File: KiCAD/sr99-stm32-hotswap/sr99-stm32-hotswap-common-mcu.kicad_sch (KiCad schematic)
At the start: 52 parts, among them J1 UDB, J2 Conn_01x02, Q1 2N7002, Q2 2N7002, Q3 2N7002, U1 STM32G474CBTx, U12 M25C-MEM-SPI, U2 MC74HC589AD, U3 MC74HC589AD, U4 MC74HC589AD, U5 AP2112K, Y1 8Mhz SMD3225-4P

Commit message: wip-2025-11-19
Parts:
- added J2: ~, Connector_JST:JST_SH_SM04B-SRSS-TB_1x04-1MP_P1.00mm_Horizontal, symbol ts-kicad-lib:QWIIC
- added J3: TC2030_SWD, PCM_marbastlib-various:CON_TC2030_outlined, symbol PCM_marbastlib-various:TC2030_SWD
- D1: footprint (none) -> Diode_SMD:D_SOD-323_HandSoldering
- renumbered C3 to C1, C9 to C10, C10 to C11, C11 to C12, C12 to C13, C13 to C14, C14 to C15, C15 to C16, C16 to C17, C17 to C18, C18 to C19, C19 to C20, C1 to C3, C38 to C9, J2 to J4, U12 to U5, U5 to U6
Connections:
- net +3V3: now also C1.2, C2.2, C3.2, J2.2, J3.1 (VCC); no longer C1.1, C10.1, C11.1, C12.1, C13.1, C14.1, C15.1, C16.1, C17.1, C18.1, C19.1, C2.1, C20.1, C3.1, C4.1, C5.1, C6.1, C7.1, C8.1, C9.1, J1.4, J1.MP, Q1.2 (S), Q2.2 (S), Q3.2 (S), R1.1, R1.3, R1.5, R1.7, R14.1, R15.1, R2.1, R2.3, R2.5, R2.7, R3.1, R3.3, R3.5, R3.7, R4.1, R4.3, R4.5, R4.7, R5.1, R5.3, R5.5, R5.7, R6.1, R9.1, U1.19 (VSSA), U1.23 (VSS), U1.35 (VSS), U1.47 (VSS), U2.14 (SA), U2.8 (GND), U3.8 (GND), U4.8 (GND), U5.4 (GND), U5.9 (Pad), U6.2 (GND), Y1.2, Y1.4
- net ~{RST}: now also J3.3 (~{RST})
- net PA13 renamed SWDIO
- net SWDIO: now also J3.2 (SWDIO)
- net PA14 renamed SWCLK
- net SWCLK: now also J3.4 (SWCLK)
- net PA15 renamed SCL
- net PB7 renamed SDA
- new net GND: C1.1, C10.1, C11.1, C12.1, C13.1, C14.1, C15.1, C16.1, C17.1, C18.1, C19.1, C2.1, C20.1, C3.1, C4.1, C5.1, C6.1, C7.1, C8.1, C9.1, J1.4, J1.MP, J2.1, J2.MP, J3.5 (GND), Q1.2 (S), Q2.2 (S), Q3.2 (S), R1.1, R1.3, R1.5, R1.7, R14.1, R15.1, R2.1, R2.3, R2.5, R2.7, R3.1, R3.3, R3.5, R3.7, R4.1, R4.3, R4.5, R4.7, R5.1, R5.3, R5.5, R5.7, R6.1, R9.1, U1.19 (VSSA), U1.23 (VSS), U1.35 (VSS), U1.47 (VSS), U2.14 (SA), U2.8 (GND), U3.8 (GND), U4.8 (GND), U5.4 (GND), U5.9 (Pad), U6.2 (GND), Y1.2, Y1.4
- new net SWSCL: J3.6 (SWO)
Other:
- note added: "Connectors"
- note removed: "UDB"
- moved on the sheet: J1

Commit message: update-2025-11-20
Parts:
- added R37, R38: 4K7, Resistor_SMD:R_0603_1608Metric, symbol Device:R_Small
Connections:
- net +3V3: now also R37.2, R38.2
- net COL0: now also R4.7; no longer R4.4
- net COL10: now also R2.8; no longer R2.2
- net COL11: now also R2.7; no longer R2.4
- net COL13: now also R2.5; no longer R2.8
- net COL14: now also R3.8; no longer R3.2
- net COL15: now also R3.7; no longer R3.4
- net COL17: now also R3.5; no longer R3.8
- net COL2: now also R4.5; no longer R4.8
- net COL3: now also R1.8; no longer R1.2
- net COL4: now also R1.7; no longer R1.4
- net COL6: now also R1.5; no longer R1.8
- net COL7: now also R5.7; no longer R5.4
- net COL9: now also R5.5; no longer R5.8
- net GND: now also R1.2, R1.3, R1.4, R2.2, R2.3, R2.4, R3.2, R3.3, R3.4, R4.2, R4.3, R4.4, R5.2, R5.3, R5.4; no longer R1.3, R1.5, R1.7, R2.3, R2.5, R2.7, R3.3, R3.5, R3.7, R4.3, R4.5, R4.7, R5.3, R5.5, R5.7
- net SCL: now also J2.4, R37.1
- net SDA: now also J2.3, R38.1
- net at U2.15 (A): now also R4.8; no longer R4.2
- net at U3.15 (A): now also R5.8; no longer R5.2
- net PB10: no longer names the net of U1.22 (PB10)
- no-connect marks 0 -> 1
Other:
- moved on the sheet: C13, C4, D1, J1, J3, J4, Q2, Q3, R10, R12, R13, R14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

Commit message: wip-2025-11-23
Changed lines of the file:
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@@
 		)
 		(property "Value" "MC74HC589AD"
-			(at 273.304 73.66 0)
+			(at 271.78 73.66 0)
 			(effects
 				(font
@@
 		)
 		(property "Value" "MC74HC589AD"
-			(at 235.204 73.66 0)
+			(at 233.68 73.66 0)
 			(effects
 				(font
@@
 		)
 		(property "Value" "MC74HC589AD"
-			(at 197.104 73.66 0)
+			(at 195.58 73.66 0)
 			(effects
 				(font

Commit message: wip
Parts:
- added J5: ~, Connector_JST:JST_SH_SM02B-SRSS-TB_1x02-1MP_P1.00mm_Horizontal, symbol ts-kicad-lib:CONN_02
- C1, C10, C11, C12, C13, C14, C15, C16, C17, C18, C19, C2, C20, C3, C5, C6, C7, C8, C9, R7: footprint Capacitor_SMD:C_0603_1608Metric -> Capacitor_SMD:C_0402_1005Metric
- R10, R11, R12, R13, R14, R15, R16, R37, R38, R8, R9: footprint Resistor_SMD:R_0603_1608Metric -> Resistor_SMD:R_0402_1005Metric
- R6: footprint Capacitor_SMD:C_0603_1608Metric -> Resistor_SMD:R_0402_1005Metric
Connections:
- net GND: now also J5.MP
- net PA0: no longer names the net of U1.8 (PA0)
- net PA1: no longer names the net of U1.9 (PA1)
- net PA10: no longer names the net of U1.32 (PA10)
- net PA2: no longer names the net of U1.10 (PA2)
- net PA3: no longer names the net of U1.11 (PA3)
- net PA4: no longer names the net of U1.12 (PA4)
- net PA5 renamed SCK
- net PA8: no longer names the net of U1.30 (PA8)
- net PA9: no longer names the net of U1.31 (PA9)
- net PB0: no longer names the net of U1.16 (PB0)
- net PB1: no longer names the net of U1.17 (PB1)
- net PB11: no longer names the net of U1.25 (PB11)
- net PB12: no longer names the net of U1.26 (PB12)
- net PB13: no longer names the net of U1.27 (PB13)
- net PB14: no longer names the net of U1.28 (PB14)
- net PB15: no longer names the net of U1.29 (PB15)
- net PB2: no longer names the net of U1.18 (PB2)
- net PB3: no longer names the net of U1.40 (PB3)
- net PB4 renamed UCPD1_CC2
- net UCPD1_CC2: now also J5.2
- net PB5: no longer names the net of U1.42 (PB5)
- net PB6 renamed UCPD1_CC1
- net UCPD1_CC1: now also J5.1
- net PB9: no longer names the net of U1.46 (PB9)
- net PC13: no longer names the net of U1.2 (PC13)
- net PC14: no longer names the net of U1.3 (PC14)
- net PC15: no longer names the net of U1.4 (PC15)
- no-connect marks 1 -> 23

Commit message: pre-DRC upload
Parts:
- removed R11: 0, Resistor_SMD:R_0402_1005Metric, symbol Device:R_Small
- added D108, D109: LED, ts-keyboard-lib:LED_MHT151C, symbol ts-kicad-lib:LED
- added NT1, NT2, NT3: NetTie_2, ts-kicad-lib:NetTie-2_SMD_Pad0.254mm, symbol ts-kicad-lib:NetTie_2
- added R39, R40: 510R, Resistor_SMD:R_0603_1608Metric, symbol Device:R_Small
- added R41: 10K, Resistor_SMD:R_0402_1005Metric, symbol ts-kicad-lib:R
- added TP1: (no value), TestPoint:TestPoint_Pad_D1.0mm, symbol ts-kicad-lib:TEST_POINT
- C1, C14, C15, C16, C17, C18, C2, C3: footprint Capacitor_SMD:C_0402_1005Metric -> Capacitor_SMD:C_0603_1608Metric
- J2, J5: value ~ -> (none)
- J3: footprint PCM_marbastlib-various:CON_TC2030_outlined -> Connector:Tag-Connect_TC2030-IDC-NL_2x03_P1.27mm_Vertical; symbol PCM_marbastlib-various:TC2030_SWD -> ts-keyboard-mcu-lib:TC2030-SWD; now left out of the parts list
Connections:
- net +3V3: now also NT1.1; no longer C8.2, U1.1 (VBAT)
- net COL7: now also R5.6; no longer R5.7
- net COL8: now also R5.7; no longer R5.6
- net EEPROM_CS: now also U1.12 (PA4)
- net GND: now also D108.1 (K), D109.1 (K), NT2.1, R41.2; no longer C10.1, C11.1, C12.1, U1.19 (VSSA), U2.14 (SA)
- net MATRIX_CS: now also U1.9 (PA1)
- net SWSCL: now also U1.40 (PB3)
- net VDDA: now also NT3.1
- net VREF+: now also NT3.2
- net NOP_1: now reaches R6.2, U4.1 (B), U4.15 (A), U4.2 (C), U4.3 (D)
- net U_3_4: now reaches U3.9 (QH), U4.14 (SA)
- net BOOT_SW: now reaches D1.2 (A), J4.2 (Pin_2), R13.1, UBOOT1.2
- net U_2_3: now reaches U2.9 (QH), U3.14 (SA)
- net ENC_C: now reaches U1.10 (PA2)
- net ENC_D: now reaches U1.11 (PA3)
- net LED2_CS: now reaches U1.16 (PB0)
- net LED1_CS: now reaches U1.17 (PB1)
- net LED_CL: now reaches U1.18 (PB2)
- net LED_CL: now also R39.2
- net LED_PWR_EN: now reaches U1.2 (PC13)
- net ROW5: now reaches U1.22 (PB10)
- net ROW4: now reaches U1.25 (PB11)
- net ROW3: now reaches U1.26 (PB12)
- net ROW2: now reaches U1.27 (PB13)
- net ROW1: now reaches U1.28 (PB14)
- net ROW0: now reaches U1.29 (PB15)
- net ENC_A: now reaches U1.3 (PC14)
- net ENC_B: now reaches U1.4 (PC15)
- net LED_NL: now reaches U1.42 (PB5)
- net LED_NL: now also R40.2
- net SYS_WKUP1: now reaches U1.8 (PA0)
- net SYS_WKUP1: now also TP1.1
- net LATCH renamed ~{MATRIX_CS}
- new net: D108.2 (A), R39.1
- new net: R41.1, U2.14 (SA)
- new net: D109.2 (A), R40.1
- new net GNDA: C10.1, C11.1, C12.1, NT2.2, U1.19 (VSSA)
- new net VBAT: C8.2, NT1.2, U1.1 (VBAT)
- no-connect marks 23 -> 4
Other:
- note added: "Power Flags"
- note added: "STM32G474CBTx"
- note removed: "** Pin assignment TBD **"
- moved on the sheet: C19, C20, J1, J2, Q1, R7

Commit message: ready to order
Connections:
- net X30: now reaches U1.30 (PA8)
- net X31: now reaches U1.31 (PA9)
- net X32: now reaches U1.32 (PA10)
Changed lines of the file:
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@@
 	)
 	(no_connect
-		(at 99.06 63.5)
+		(at 104.14 63.5)
 	)
 	(no_connect
@@
 	)
 	(no_connect
-		(at 99.06 60.96)
+		(at 104.14 60.96)
 	)
 	(no_connect
-		(at 99.06 66.04)
+		(at 104.14 66.04)
 	)
 	(wire
@@
 	(wire
 		(pts
-			(xy 96.52 66.04) (xy 99.06 66.04)
+			(xy 96.52 66.04) (xy 104.14 66.04)
 		)
 		(stroke
@@
 	(wire
 		(pts
-			(xy 96.52 63.5) (xy 99.06 63.5)
+			(xy 96.52 63.5) (xy 104.14 63.5)
 		)
 		(stroke
@@
 	(wire
 		(pts
-			(xy 96.52 60.96) (xy 99.06 60.96)
+			(xy 96.52 60.96) (xy 104.14 60.96)
 		)
 		(stroke
@@
 		)
 	)
+	(label "X31"
+		(at 97.79 63.5 0)
+		(effects
+			(font
+				(size 1.27 1.27)
+			)
+			(justify left bottom)
+		)
+	)
 	(label "~{MATRIX_CS}"
 		(at 182.88 93.98 0)
@@
 		)
 	)
+	(label "X30"
+		(at 97.79 66.04 0)
+		(effects
+			(font
+				(size 1.27 1.27)
+			)
+			(justify left bottom)
+		)
+	)
 	(label "NOP_1"
 		(at 267.97 58.42 0)
@@
 			)
 			(justify left bottom)
+		)
+	)
+	(label "X32"
+		(at 97.79 60.96 0)
+		(effects
+			(font
+				(size 1.27 1.27)
+			)
+			(justify left bottom)

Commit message: .
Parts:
- added J6: Conn_01x06_Socket, ts-kicad-lib:Tag-Connect_EC-06-IDC_P1.27mm_Vertical, symbol Connector:Conn_01x06_Socket
- J3: footprint Connector:Tag-Connect_TC2030-IDC-NL_2x03_P1.27mm_Vertical -> ts-kicad-lib:Tag-Connect_TC2030-IDC-NL_2x03_P1.27mm_Vertical
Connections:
- net +3V3: now also J6.1 (Pin_1)
- net GND: now also J6.5 (Pin_5)
- net SWCLK: now also J6.4 (Pin_4)
- net SWDIO: now also J6.2 (Pin_2)
- net SWSCL: now also J6.6 (Pin_6)
- net ~{RST}: now also J6.3 (Pin_3)
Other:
- moved on the sheet: C10, C11, C12, FB1, NT2, NT3

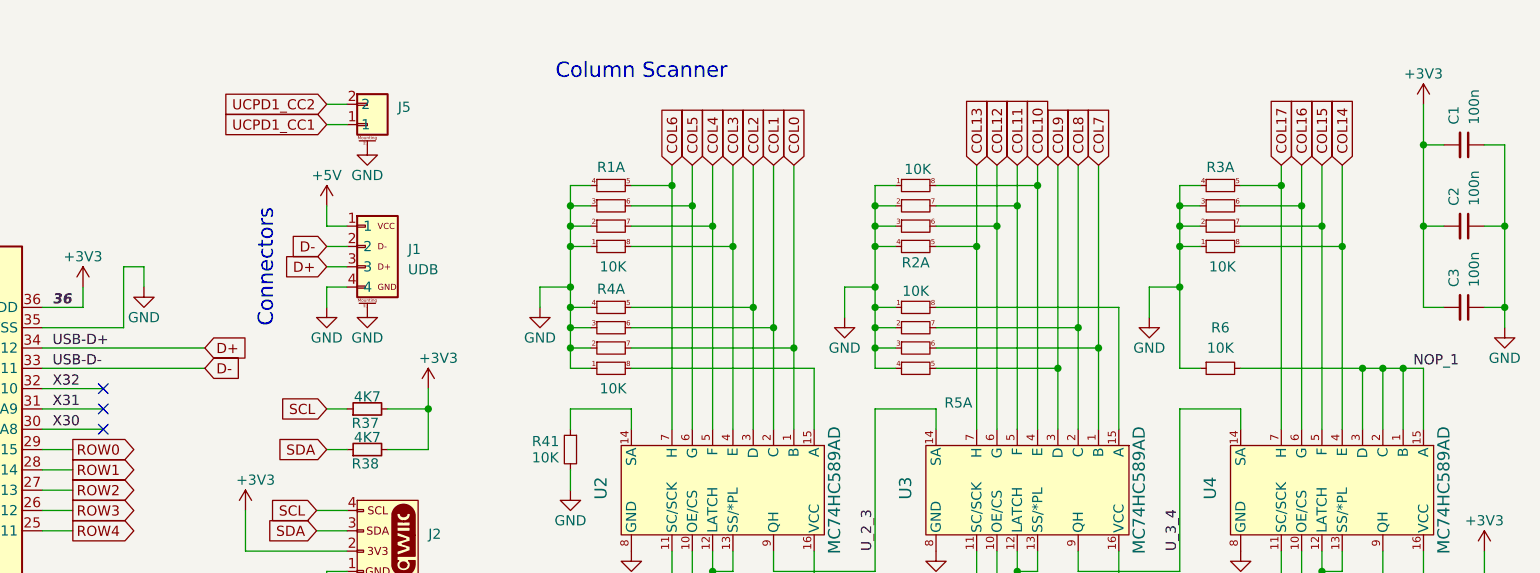
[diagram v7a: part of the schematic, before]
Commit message: Added Tag-Connect EC-06
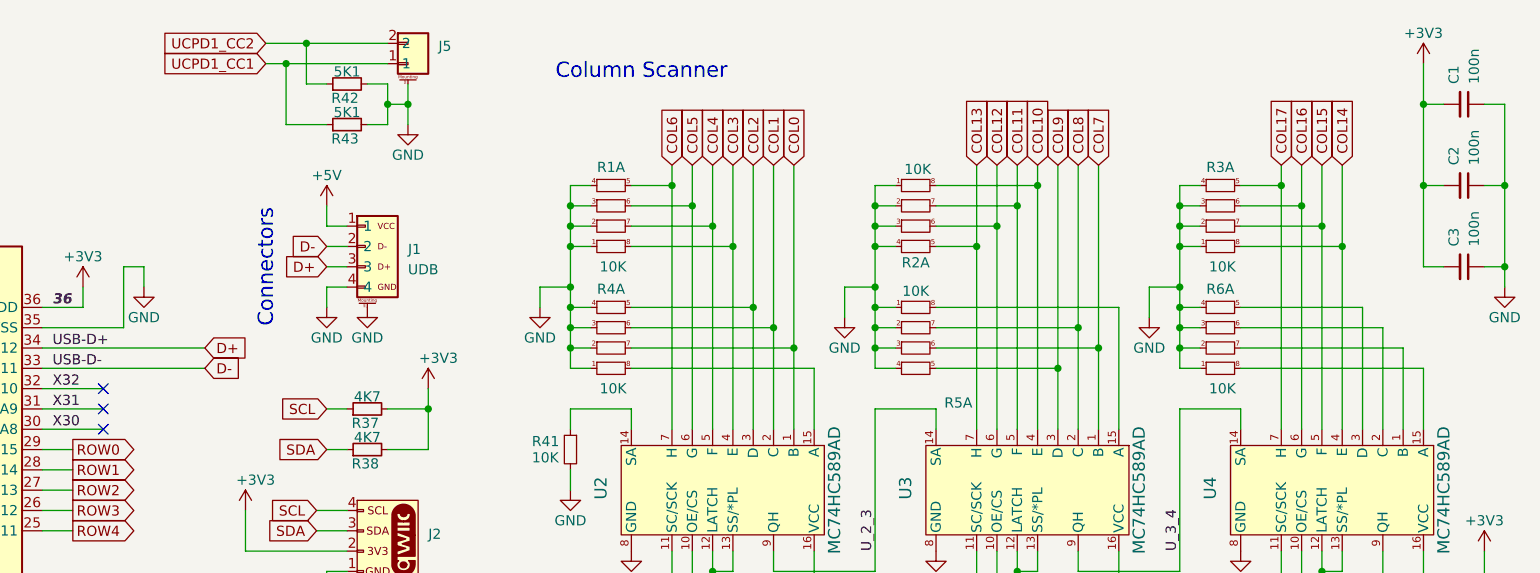
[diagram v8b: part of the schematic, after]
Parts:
- removed R6: 10K, Resistor_SMD:R_0402_1005Metric, symbol ts-kicad-lib:R
- added R42, R43: 5K1, Resistor_SMD:R_0402_1005Metric, symbol Device:R_Small
- added R6: 10K, Resistor_SMD:R_Array_Convex_4x0603, symbol ts-kicad-lib:R_Array04
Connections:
- net GND: now also R42.2, R43.2, R6.1, R6.2, R6.3, R6.4
- net UCPD1_CC1: now also R43.1
- net UCPD1_CC2: now also R42.1
- removed net NOP_1: U4.1 (B), U4.15 (A), U4.2 (C), U4.3 (D)
- new net: R6.7, U4.1 (B)
- new net: R6.8, U4.15 (A)
- new net: R6.6, U4.2 (C)
- new net: R6.5, U4.3 (D)
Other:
- moved on the sheet: C1, C2, C3, J5
